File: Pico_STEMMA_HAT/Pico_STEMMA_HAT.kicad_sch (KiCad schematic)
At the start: 46 parts, among them J1 Conn_01x20_Socket, J2 Conn_01x20_Socket, J3 SDCARD_MODULE, U1 Neopixel

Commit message: Fix SD Card connections
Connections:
- net GPIO17/CARD_DETECT: no longer J1.19 (Pin_19)
- net GPIO20/MISO: no longer J3.7 (DAT0), R23.2
- net GPIO15/CS renamed GPIO17/CS
- net GPIO17/CS: now also J1.19 (Pin_19); no longer J2.20 (Pin_20)
- net GPIO16/DEC renamed GPIO16/DATA_OUT
- net GPIO16/DATA_OUT: now also J3.7 (DAT0), R23.2
- new net GPIO15/CARD_DET: J2.20 (Pin_20)
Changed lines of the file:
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@@
 	)
 	(no_connect
+		(at 215.9 63.5)
+	)
+	(no_connect
 		(at 215.9 43.18)
 	)
@@
 	)
 	(no_connect
-		(at 215.9 76.2)
-	)
-	(no_connect
 		(at 177.8 38.1)
 	)
@@
 	(wire
 		(pts
+			(xy 49.53 48.26) (xy 86.36 48.26)
+		)
+		(stroke
+			(width 0)
+			(type default)
+		)
+	)
+	(wire
+		(pts
 			(xy 311.15 137.16) (xy 318.77 137.16)
 		)
@@
 	(wire
 		(pts
-			(xy 86.36 48.26) (xy 49.53 48.26)
-		)
-		(stroke
-			(width 0)
-			(type default)
-		)
-	)
-	(wire
-		(pts
 			(xy 173.99 48.26) (xy 177.8 48.26)
 		)
@@
 	(wire
 		(pts
-			(xy 86.36 45.72) (xy 57.15 45.72)
-		)
-		(stroke
-			(width 0)
-			(type default)
-		)
-	)
-	(wire
-		(pts
 			(xy 173.99 68.58) (xy 177.8 68.58)
 		)
@@
 	(wire
 		(pts
+			(xy 57.15 45.72) (xy 86.36 45.72)
+		)
+		(stroke
+			(width 0)
+			(type default)
+		)
+	)
+	(wire
+		(pts
 			(xy 314.96 97.79) (xy 314.96 110.49)
 		)
@@
 		)
 	)
-	(label "GPIO20{slash}MISO"
-		(at 74.93 45.72 0)
+	(label "GPIO16{slash}DATA_OUT"
+		(at 69.85 45.72 0)
 		(fields_autoplaced yes)
 		(effects
@@
 		)
 	)
-	(label "GPIO16{slash}DEC"
+	(label "GPIO16{slash}DATA_OUT"
 		(at 215.9 76.2 180)
 		(fields_autoplaced yes)
@@
 		)
 	)
-	(label "GPIO17{slash}CARD_DETECT"
+	(label "GPIO17{slash}CS"
 		(at 215.9 73.66 180)
 		(fields_autoplaced yes)
@@
 	)
 	(label "GPIO21{slash}DAT1"
-		(at 77.47 48.26 0)
+		(at 73.66 48.26 0)
 		(fields_autoplaced yes)
 		(effects
@@
 		)
 	)
-	(label "GPIO15{slash}CS"
+	(label "GPIO15{slash}CARD_DET"
 		(at 177.8 76.2 0)
 		(fields_autoplaced yes)
@@
 		)
 	)
-	(label "GPIO15{slash}CS"
+	(label "GPIO17{slash}CS"
 		(at 69.85 53.34 0)
 		(fields_autoplaced yes)

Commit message: Adjust silkscreen
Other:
- moved on the sheet: D1, R17
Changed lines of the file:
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@@
 	(wire
 		(pts
-			(xy 238.76 137.16) (xy 238.76 139.7)
+			(xy 238.76 135.89) (xy 238.76 138.43)
 		)
 		(stroke
@@
 	(wire
 		(pts
-			(xy 238.76 147.32) (xy 238.76 149.86)
+			(xy 238.76 146.05) (xy 238.76 148.59)
 		)
 		(stroke
@@
 	(wire
 		(pts
-			(xy 238.76 157.48) (xy 238.76 161.29)
+			(xy 238.76 156.21) (xy 238.76 160.02)
 		)
 		(stroke
@@
 	)
 	(rectangle
+		(start 232.41 125.73)
+		(end 246.38 166.37)
+		(stroke
+			(width 0)
+			(type default)
+		)
+		(fill
+			(type none)
+		)
+	)
+	(rectangle
 		(start 165.1 88.9)
 		(end 228.6 166.37)
@@
 	(text "POWER LED"
 		(exclude_from_sim no)
-		(at 239.014 130.048 0)
+		(at 239.014 128.778 0)
 		(effects
 			(font
@@
 	(symbol
 		(lib_id "power:+3V3")
-		(at 238.76 137.16 0)
+		(at 238.76 135.89 0)
 		(unit 1)
 		(exclude_from_sim no)
@@
 		(fields_autoplaced yes)
 		(property "Reference" "#PWR053"
-			(at 238.76 140.97 0)
+			(at 238.76 139.7 0)
 			(effects
 				(font
@@
 		)
 		(property "Value" "+3V3"
-			(at 238.76 132.08 0)
+			(at 238.76 130.81 0)
 			(effects
 				(font
@@
 		)
 		(property "Footprint" ""
-			(at 238.76 137.16 0)
+			(at 238.76 135.89 0)
 			(effects
 				(font
@@
 		)
 		(property "Datasheet" ""
-			(at 238.76 137.16 0)
+			(at 238.76 135.89 0)
 			(effects
 				(font
@@
 		)
 		(property "Description" "Power symbol creates a global label with name \"+3V3\""
-			(at 238.76 137.16 0)
+			(at 238.76 135.89 0)
 			(effects
 				(font
@@
 	(symbol
 		(lib_id "Device:R_US")
-		(at 238.76 143.51 0)
+		(at 238.76 142.24 0)
 		(unit 1)
 		(exclude_from_sim no)
@@
 		(fields_autoplaced yes)
 		(property "Reference" "R17"
-			(at 241.3 142.2399 0)
+			(at 241.3 140.9699 0)
 			(effects
 				(font
@@
 		)
 		(property "Value" "10k"
-			(at 241.3 144.7799 0)
+			(at 241.3 143.5099 0)
 			(effects
 				(font
@@
 		)
 		(property "Footprint" "Resistor_SMD:R_0603_1608Metric"
-			(at 239.776 143.764 90)
+			(at 239.776 142.494 90)
 			(effects
 				(font
@@
 		)
 		(property "Datasheet" "~"
-			(at 238.76 143.51 0)
+			(at 238.76 142.24 0)
 			(effects
 				(font
@@
 		)
 		(property "Description" "Resistor, US symbol"
-			(at 238.76 143.51 0)
+			(at 238.76 142.24 0)
 			(effects
 				(font
@@
 	(symbol
 		(lib_id "Device:LED")
-		(at 238.76 153.67 90)
+		(at 238.76 152.4 90)
 		(unit 1)
 		(exclude_from_sim no)
@@
 		(fields_autoplaced yes)
 		(property "Reference" "D1"
-			(at 242.57 153.9874 90)
+			(at 242.57 152.7174 90)
 			(effects
 				(font
@@
 		)
 		(property "Value" "LED"
-			(at 242.57 156.5274 90)
+			(at 242.57 155.2574 90)
 			(effects
 				(font
@@
 		)
 		(property "Footprint" "LED_SMD:LED_0603_1608Metric"
-			(at 238.76 153.67 0)
+			(at 238.76 152.4 0)
 			(effects
 				(font
@@
 		)
 		(property "Datasheet" "~"
-			(at 238.76 153.67 0)
+			(at 238.76 152.4 0)
 			(effects
 				(font
@@
 		)
 		(property "Description" "Light emitting diode"
-			(at 238.76 153.67 0)
+			(at 238.76 152.4 0)
 			(effects
 				(font
@@
 	(symbol
 		(lib_id "power:GND")
-		(at 238.76 161.29 0)
+		(at 238.76 160.02 0)
 		(unit 1)
 		(exclude_from_sim no)
@@
 		(fields_autoplaced yes)
 		(property "Reference" "#PWR054"
-			(at 238.76 167.64 0)
+			(at 238.76 166.37 0)
 			(effects
 				(font
@@
 		)
 		(property "Value" "GND"
-			(at 238.76 166.37 0)
+			(at 238.76 165.1 0)
 			(effects
 				(font
@@
 		)
 		(property "Footprint" ""
-			(at 238.76 161.29 0)
+			(at 238.76 160.02 0)
 			(effects
 				(font
@@
 		)
 		(property "Datasheet" ""
-			(at 238.76 161.29 0)
+			(at 238.76 160.02 0)
 			(effects
 				(font
@@
 		)
 		(property "Description" "Power symbol creates a global label with name \"GND\" , ground"
-			(at 238.76 161.29 0)
+			(at 238.76 160.02 0)
 			(effects
 				(font

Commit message: Add decoupling cap for the SD card reader
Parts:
- added C10: 0.1 uF, Capacitor_SMD:C_0603_1608Metric, symbol Device:C
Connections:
- net +3V3: now also C10.1
- net GND: now also C10.2
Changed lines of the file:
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@@
 	(wire
 		(pts
+			(xy 20.32 66.04) (xy 20.32 71.12)
+		)
+		(stroke
+			(width 0)
+			(type default)
+		)
+	)
+	(wire
+		(pts
 			(xy 294.64 74.93) (xy 294.64 80.01)
 		)
@@
 	(wire
 		(pts
+			(xy 20.32 78.74) (xy 20.32 81.28)
+		)
+		(stroke
+			(width 0)
+			(type default)
+		)
+	)
+	(wire
+		(pts
 			(xy 389.89 39.37) (xy 389.89 44.45)
 		)
@@
 		)
 	)
+	(text "DECOUPlING CAP"
+		(exclude_from_sim no)
+		(at 25.654 73.66 90)
+		(effects
+			(font
+				(size 1.27 1.27)
+			)
+		)
+	)
 	(text "TCA9548A CONNECTIONS"
 		(exclude_from_sim no)
@@
 	)
 	(symbol
+		(lib_id "Device:C")
+		(at 20.32 74.93 0)
+		(unit 1)
+		(exclude_from_sim no)
+		(in_bom yes)
+		(on_board yes)
+		(dnp no)
+		(property "Reference" "C10"
+			(at 18.542 77.724 0)
+			(effects
+				(font
+					(size 1.27 1.27)
+				)
+				(justify left)
+			)
+		)
+		(property "Value" "0.1 uF"
+			(at 18.542 80.264 0)
+			(effects
+				(font
+					(size 1.27 1.27)
+				)
+				(justify left)
+			)
+		)
+		(property "Footprint" "Capacitor_SMD:C_0603_1608Metric"
+			(at 21.2852 78.74 0)
+			(effects
+				(font
+					(size 1.27 1.27)
+				)
+				(hide yes)
+			)
+		)
+		(property "Datasheet" "~"
+			(at 20.32 74.93 0)
+			(effects
+				(font
+					(size 1.27 1.27)
+				)
+				(hide yes)
+			)
+		)
+		(property "Description" "Unpolarized capacitor"
+			(at 20.32 74.93 0)
+			(effects
+				(font
+					(size 1.27 1.27)
+				)
+				(hide yes)
+			)
+		)
+		(pin "1"
+		)
+		(pin "2"
+		)
+		(instances
+			(project "Pico_STEMMA_HAT"
+				(path "/d7f0761f-a3d3-4a87-8eca-6574a8f4791b"
+					(reference "C10")
+					(unit 1)
+				)
+			)
+		)
+	)
+	(symbol
 		(lib_id "power:+3V3")
 		(at 318.77 26.67 0)
@@
 	)
 	(symbol
+		(lib_id "power:GND")
+		(at 20.32 81.28 0)
+		(unit 1)
+		(exclude_from_sim no)
+		(in_bom yes)
+		(on_board yes)
+		(dnp no)
+		(fields_autoplaced yes)
+		(property "Reference" "#PWR068"
+			(at 20.32 87.63 0)
+			(effects
+				(font
+					(size 1.27 1.27)
+				)
+				(hide yes)
+			)
+		)
+		(property "Value" "GND"
+			(at 20.32 86.36 0)
+			(effects
+				(font
+					(size 1.27 1.27)
+				)
+			)
+		)
+		(property "Footprint" ""
+			(at 20.32 81.28 0)
+			(effects
+				(font
+					(size 1.27 1.27)
+				)
+				(hide yes)
+			)
+		)
+		(property "Datasheet" ""
+			(at 20.32 81.28 0)
+			(effects
+				(font
+					(size 1.27 1.27)
+				)
+				(hide yes)
+			)
+		)
+		(property "Description" "Power symbol creates a global label with name \"GND\" , ground"
+			(at 20.32 81.28 0)
+			(effects
+				(font
+					(size 1.27 1.27)
+				)
+				(hide yes)
+			)
+		)
+		(pin "1"
+		)
+		(instances
+			(project "Pico_STEMMA_HAT"
+				(path "/d7f0761f-a3d3-4a87-8eca-6574a8f4791b"
+					(reference "#PWR068")
+					(unit 1)
+				)
+			)
+		)
+	)
+	(symbol
 		(lib_id "Device:C")
 		(at 346.71 107.95 0)
@@
 					(unit 1)
 				)
+			)
+		)
+	)
+	(symbol
+		(lib_id "power:+3V3")
+		(at 20.32 66.04 0)
+		(unit 1)
+		(exclude_from_sim no)
+		(in_bom yes)
+		(on_board yes)
+		(dnp no)
+		(property "Reference" "#PWR067"
+			(at 20.32 69.85 0)
+			(effects
+				(font
+					(size 1.27 1.27)
+				)
+				(hide yes)
+			)
+		)
+		(property "Value" "+3V3"
+			(at 22.352 68.326 90)
+			(effects
+				(font
+					(size 1.27 1.27)
+				)
+			)
+		)
+		(property "Footprint" ""
+			(at 20.32 66.04 0)
+			(effects
+				(font
+					(size 1.27 1.27)
+				)
+				(hide yes)
+			)
+		)
+		(property "Datasheet" ""
+			(at 20.32 66.04 0)
+			(effects
+				(font
+					(size 1.27 1.27)
+				)
+				(hide yes)
+			)
+		)
+		(property "Description" "Power symbol creates a global label with name \"+3V3\""
+			(at 20.32 66.04 0)
+			(effects
+				(font
+					(size 1.27 1.27)
+				)
+				(hide yes)
+			)
+		)
+		(pin "1"
+		)
+		(instances
+			(project "Pico_STEMMA_HAT"
+				(path "/d7f0761f-a3d3-4a87-8eca-6574a8f4791b"
+					(reference "#PWR067")
+					(unit 1)
+				)

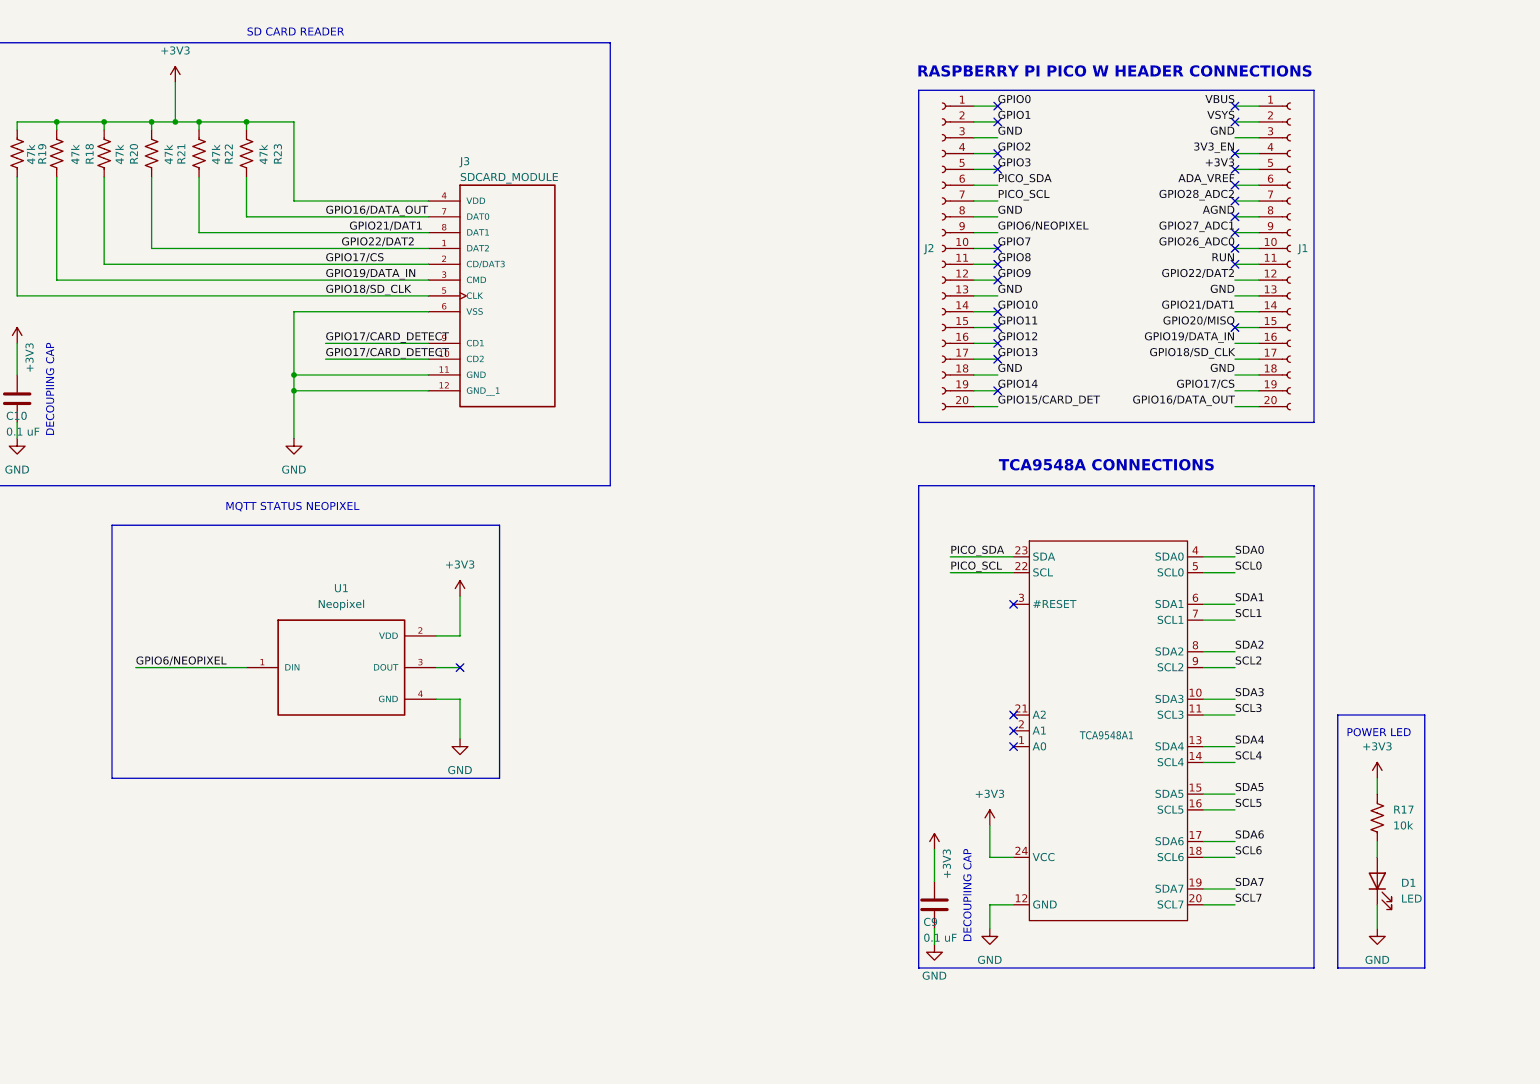
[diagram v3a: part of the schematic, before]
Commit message: Fix pull-up resistors for multiplexer
Add the pull-up resistors from the schem to the PCB design. Adjusted resistor value for red LED. Adjusted Neopixel footprint.
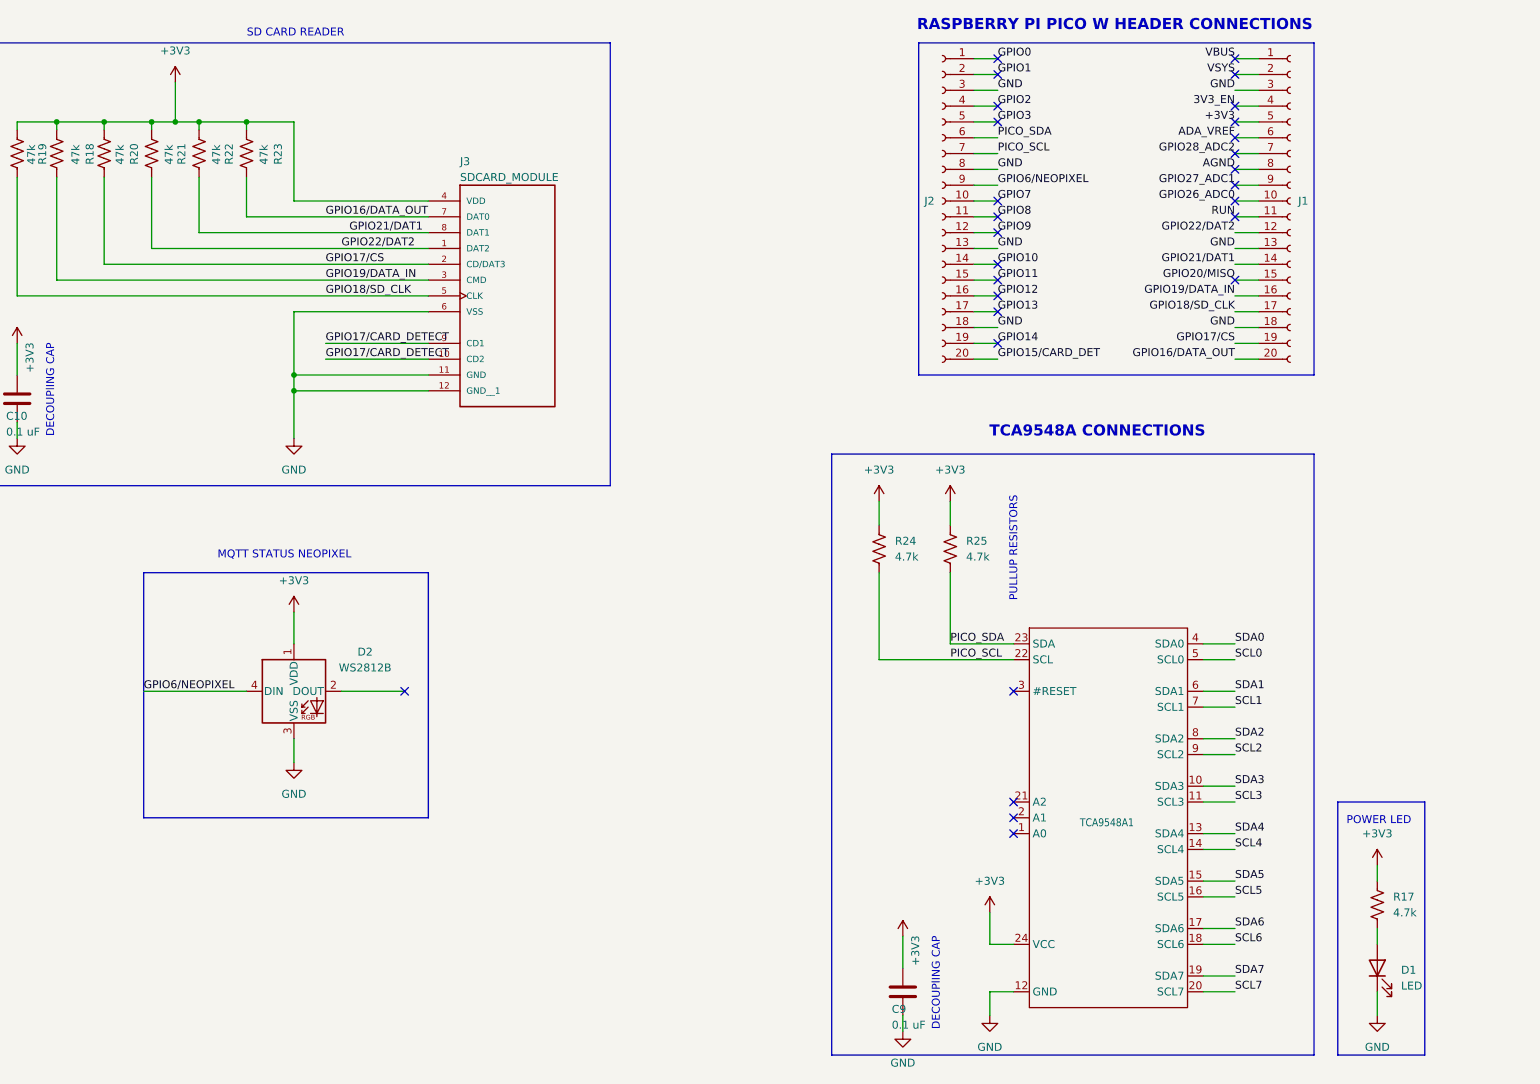
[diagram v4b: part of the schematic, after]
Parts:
- removed U1: Neopixel, Pico_Footprints:NEOPIXEL_Footprint, symbol Pico_Symbols:NEOPIXEL
- added D2: WS2812B, LED_SMD:LED_WS2812B_PLCC4_5.0x5.0mm_P3.2mm, symbol LED:WS2812B
- added R24, R25: 4.7k, Resistor_SMD:R_0603_1608Metric, symbol Device:R_US
- R17: value 10k -> 4.7k
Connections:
- net +3V3: now also D2.1 (VDD), R24.1, R25.1
- net GND: now also D2.3 (VSS)
- net GPIO6/NEOPIXEL: now also D2.4 (DIN)
- net PICO_SCL: now also R24.2
- net PICO_SDA: now also R25.2
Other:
- moved on the sheet: C9, D1, J1, J2, R17, TCA9548A1

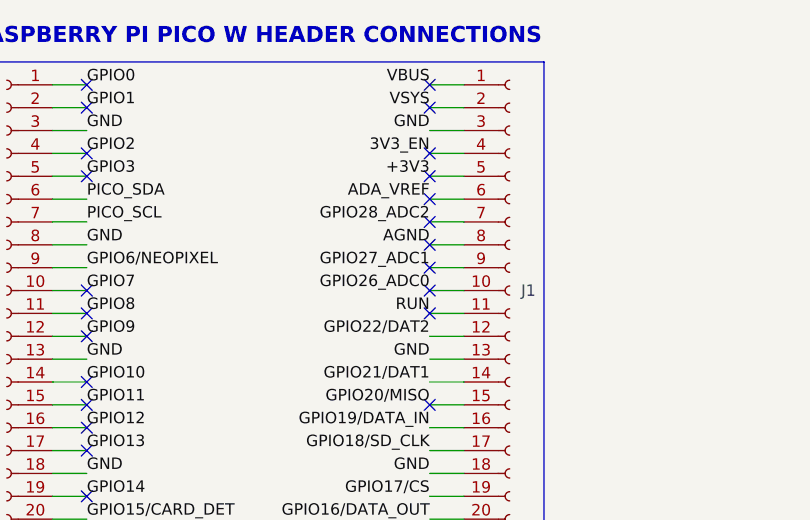
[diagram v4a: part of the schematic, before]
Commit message: Adjust silkscreen
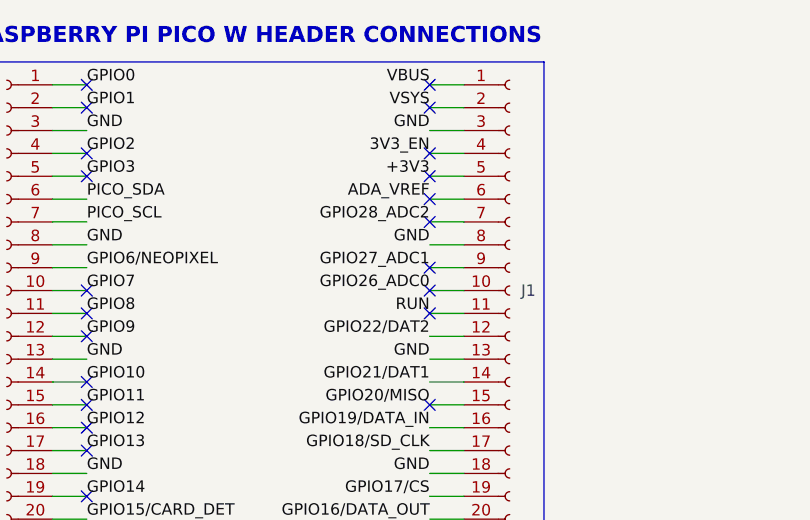
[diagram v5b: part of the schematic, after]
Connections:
- net AGND is gone; now on net GND: J1.8 (Pin_8)
- no-connect marks 28 -> 27
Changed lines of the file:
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@@
-	)
-	(no_connect
-		(at 215.9 38.1)
 	)
 	(no_connect
@@
 		)
 	)
-	(label "AGND"
+	(label "GND"
 		(at 215.9 38.1 180)
 		(fields_autoplaced yes)
